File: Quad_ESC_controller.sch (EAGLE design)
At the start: 23 parts, among them Y1 ECS-80-S-4X

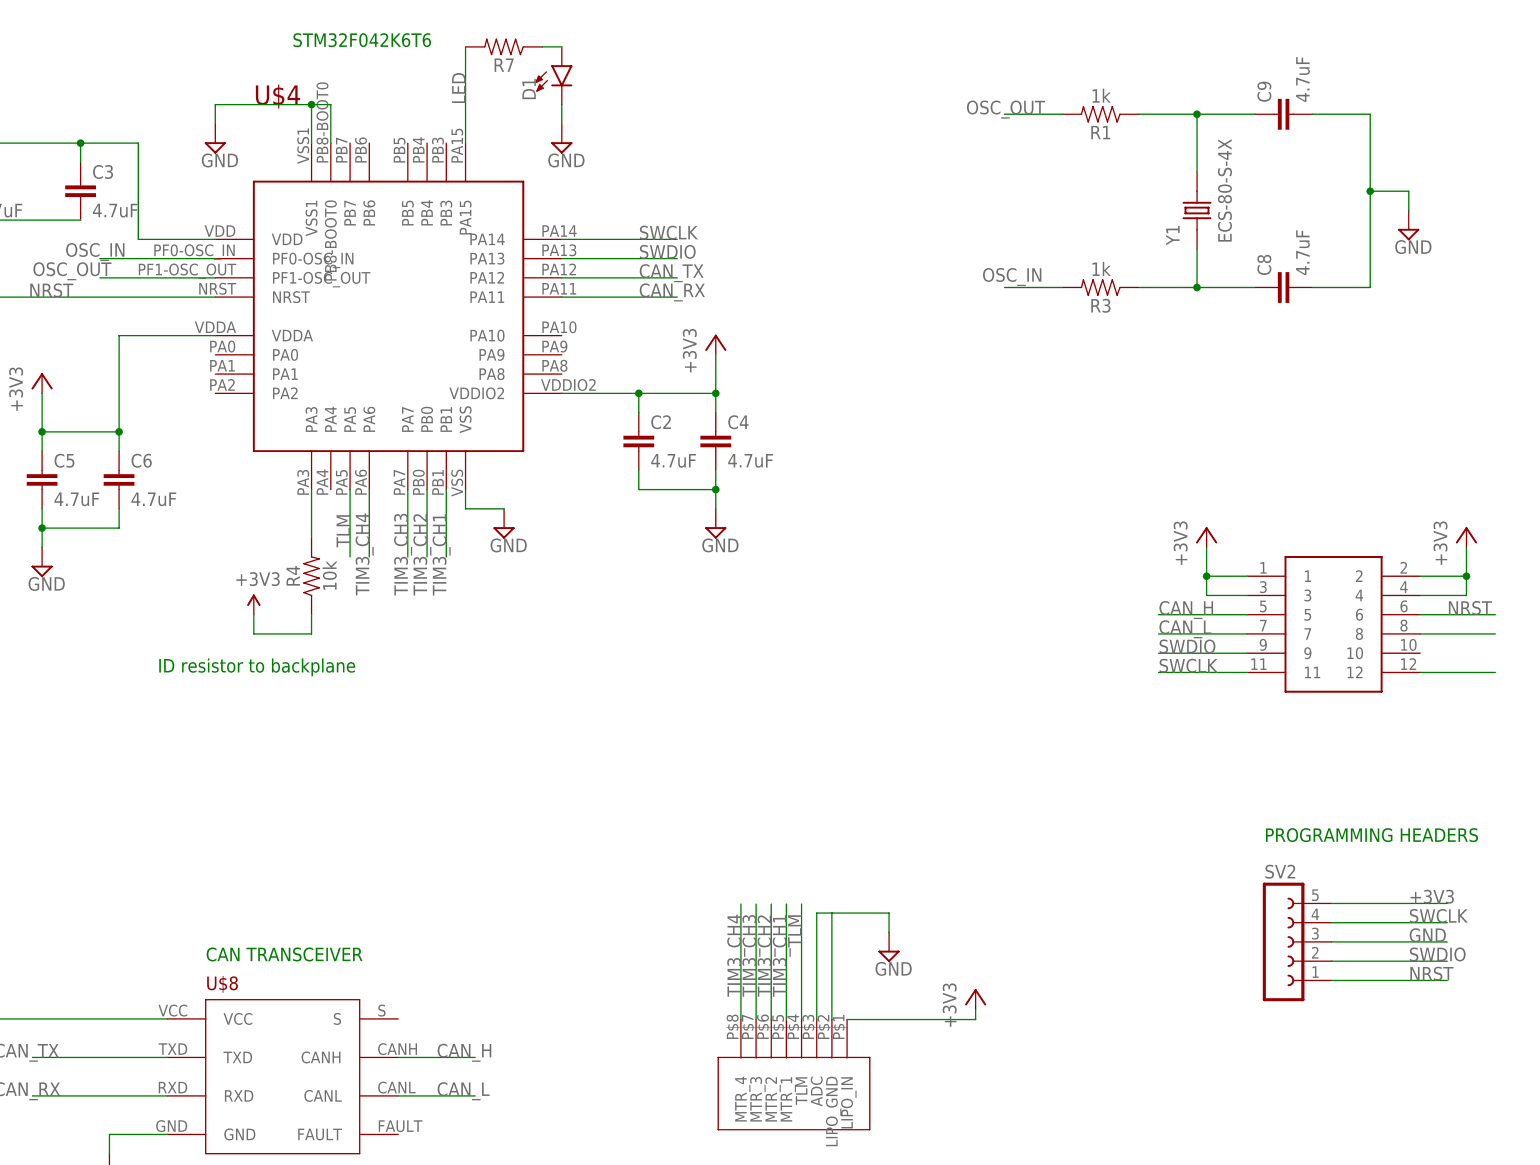
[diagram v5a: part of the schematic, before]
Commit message: Final Board Changes   ✽-(ˆ▿ˆ)/✽
thank god

(changes: vias con. to GND, esc id/tlm connections, design moved, connector footprint replaced, font sizes changed)
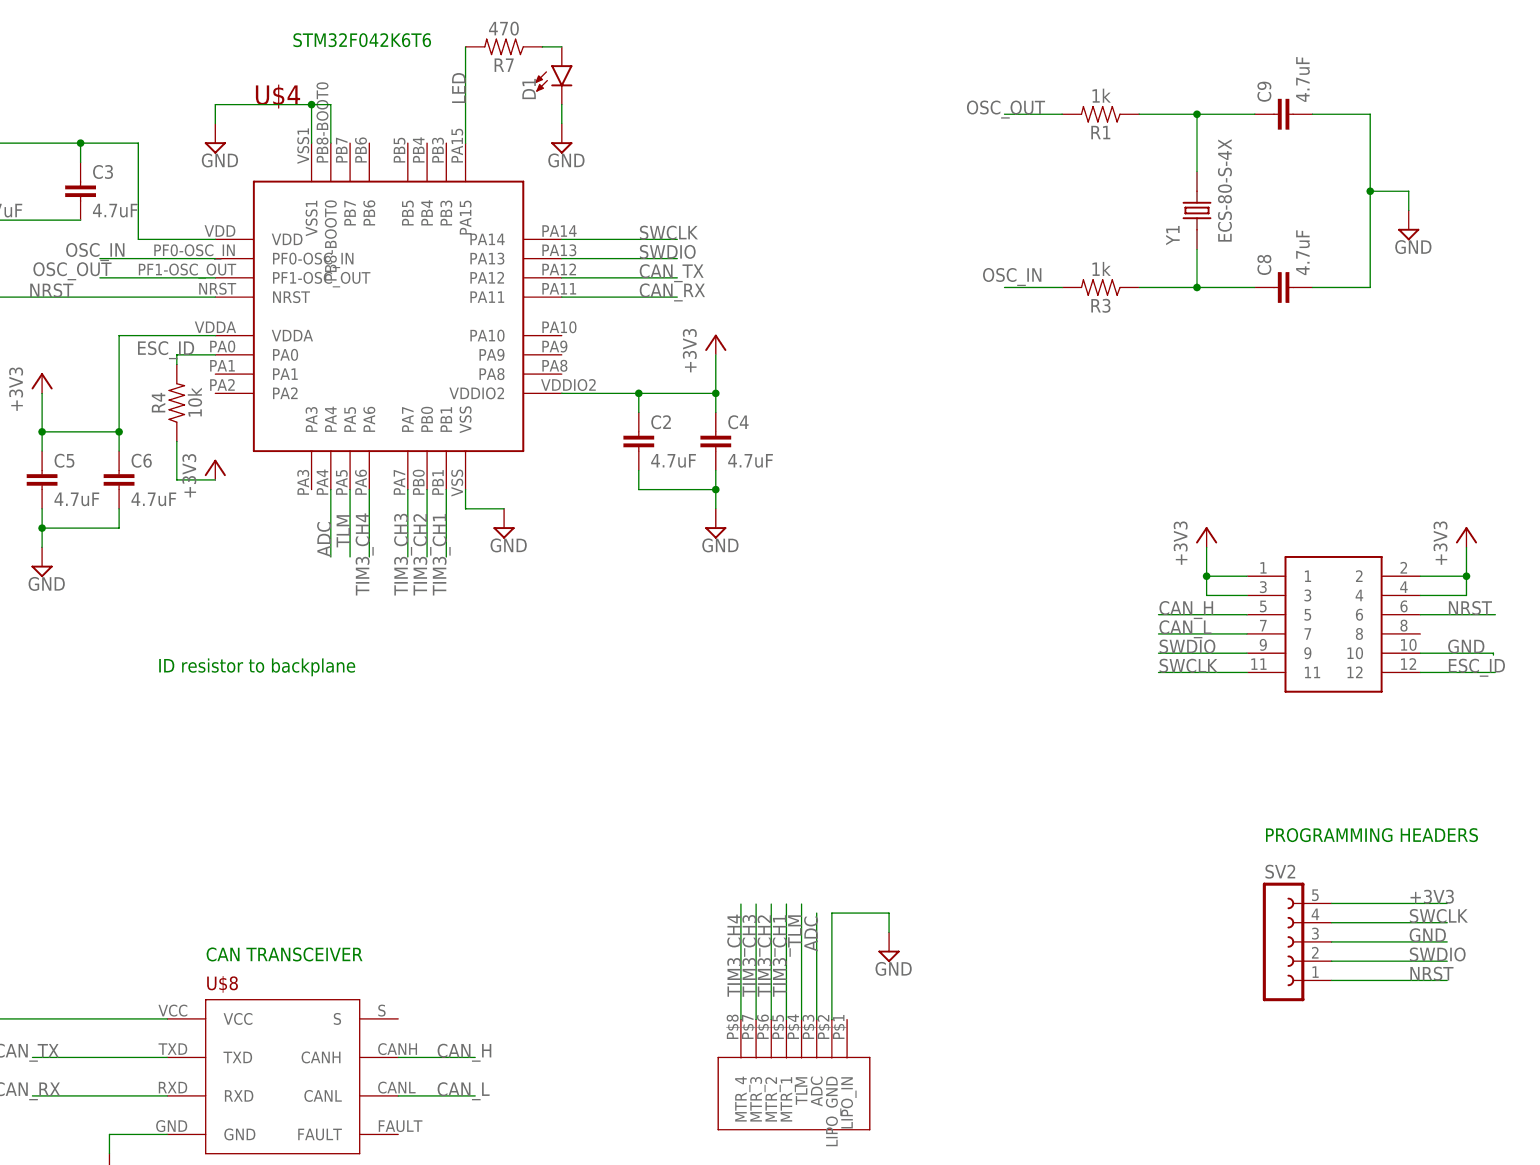
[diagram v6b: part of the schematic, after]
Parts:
- R7: value (none) -> 470
- RESET: value SWITCH -> DISCRETECOMPONENTS_SWITCH; device DiscreteComponents:SWITCH -> Push button - FSM2JMTR:DISCRETECOMPONENTS_SWITCH
- U$3: value BACKPLANE_CONNECTORSBKP -> BACKPLANE_CONNECTORSESC; device BLHeli_32 45A:BACKPLANE_CONNECTORSBKP -> BLHeli_32 45A:BACKPLANE_CONNECTORSESC
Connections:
- removed net N$3: R4.2, U$4.PA3
- removed net N$7: U$3.8
- removed net N$8: U$3.12
- new net ADC: U$2.ADC, U$4.PA4
- new net ESC_ID: R4.2, U$3.12, U$4.PA0
- net +3V3: no longer U$2.LIPO_IN
- net GND: now also U$3.10; no longer U$2.ADC
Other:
- moved on the sheet: R4

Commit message: JST part
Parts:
- C10: value 100nF -> 0.1uF
- C8, C9: value 4.7uF -> 20pF
- R1, R3: value 1k -> 0
- U$2: value 8PIN_CONNECTOR -> JST-8PIN; device BLHeli_32 45A:8PIN_CONNECTOR -> JST 8 pin:JST-8PIN
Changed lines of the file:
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@@
 <layers>
 <layer number="1" name="Top" color="4" fill="1" visible="no" active="no"/>
+<layer number="2" name="Route2" color="16" fill="1" visible="no" active="no"/>
+<layer number="3" name="Route3" color="17" fill="1" visible="no" active="no"/>
+<layer number="4" name="Route4" color="18" fill="1" visible="no" active="no"/>
+<layer number="5" name="Route5" color="19" fill="1" visible="no" active="no"/>
+<layer number="6" name="Route6" color="25" fill="1" visible="no" active="no"/>
+<layer number="7" name="Route7" color="26" fill="1" visible="no" active="no"/>
+<layer number="8" name="Route8" color="27" fill="1" visible="no" active="no"/>
+<layer number="9" name="Route9" color="28" fill="1" visible="no" active="no"/>
+<layer number="10" name="Route10" color="29" fill="1" visible="no" active="no"/>
+<layer number="11" name="Route11" color="30" fill="1" visible="no" active="no"/>
+<layer number="12" name="Route12" color="20" fill="1" visible="no" active="no"/>
+<layer number="13" name="Route13" color="21" fill="1" visible="no" active="no"/>
+<layer number="14" name="Route14" color="22" fill="1" visible="no" active="no"/>
+<layer number="15" name="Route15" color="23" fill="1" visible="no" active="no"/>
 <layer number="16" name="Bottom" color="1" fill="1" visible="no" active="no"/>
 <layer number="17" name="Pads" color="2" fill="1" visible="no" active="no"/>
@@
 <part name="SV2" library="con-lsta" library_urn="urn:adsk.eagle:library:161" deviceset="FE05-1" device="" package3d_urn="urn:adsk.eagle:package:8190/1"/>
 <part name="U$8" library="PI_Shield_Library" deviceset="TCAN337D" device=""/>
-<part name="C10" library="SparkFun-Capacitors" library_urn="urn:adsk.eagle:library:510" deviceset="4.7UF" device="0603" package3d_urn="urn:adsk.eagle:package:37414/1" value="100nF"/>
+<part name="C10" library="SparkFun-Capacitors" library_urn="urn:adsk.eagle:library:510" deviceset="4.7UF" device="0603" package3d_urn="urn:adsk.eagle:package:37414/1" value="0.1uF"/>
 <part name="+3V3" library="supply1" library_urn="urn:adsk.eagle:library:371" deviceset="+3V3" device=""/>
 <part name="GND9" library="supply2" library_urn="urn:adsk.eagle:library:372" deviceset="GND" device=""/>
 <part name="GND12" library="supply2" library_urn="urn:adsk.eagle:library:372" deviceset="GND" device=""/>
-<part name="C8" library="SparkFun-Capacitors" library_urn="urn:adsk.eagle:library:510" deviceset="4.7UF" device="0603" package3d_urn="urn:adsk.eagle:package:37414/1" value="4.7uF"/>
-<part name="C9" library="SparkFun-Capacitors" library_urn="urn:adsk.eagle:library:510" deviceset="4.7UF" device="0603" package3d_urn="urn:adsk.eagle:package:37414/1" value="4.7uF"/>
+<part name="C8" library="SparkFun-Capacitors" library_urn="urn:adsk.eagle:library:510" deviceset="4.7UF" device="0603" package3d_urn="urn:adsk.eagle:package:37414/1" value="20pF"/>
+<part name="C9" library="SparkFun-Capacitors" library_urn="urn:adsk.eagle:library:510" deviceset="4.7UF" device="0603" package3d_urn="urn:adsk.eagle:package:37414/1" value="20pF"/>
 <part name="Y1" library="ECS-80-S-4X" deviceset="ECS-80-S-4X" device=""/>
-<part name="R1" library="SparkFun-Resistors" library_urn="urn:adsk.eagle:library:532" deviceset="1KOHM" device="-0603-1/10W-1%" package3d_urn="urn:adsk.eagle:package:39650/1" value="1k"/>
-<part name="R3" library="SparkFun-Resistors" library_urn="urn:adsk.eagle:library:532" deviceset="1KOHM" device="-0603-1/10W-1%" package3d_urn="urn:adsk.eagle:package:39650/1" value="1k"/>
+<part name="R1" library="SparkFun-Resistors" library_urn="urn:adsk.eagle:library:532" deviceset="1KOHM" device="-0603-1/10W-1%" package3d_urn="urn:adsk.eagle:package:39650/1" value="0"/>
+<part name="R3" library="SparkFun-Resistors" library_urn="urn:adsk.eagle:library:532" deviceset="1KOHM" device="-0603-1/10W-1%" package3d_urn="urn:adsk.eagle:package:39650/1" value="0"/>
 <part name="GND15" library="supply2" library_urn="urn:adsk.eagle:library:372" deviceset="GND" device=""/>
 <part name="R4" library="SparkFun-Resistors" library_urn="urn:adsk.eagle:library:532" deviceset="10KOHM" device="-0603-1/10W-1%" package3d_urn="urn:adsk.eagle:package:39650/1" value="10k"/>
-<part name="U$2" library="BLHeli_32 45A" deviceset="8PIN_CONNECTOR" device=""/>
+<part name="U$2" library="JST 8 pin" deviceset="JST-8PIN" device="" package3d_urn="urn:adsk.eagle:package:25902943/3"/>
 <part name="U$3" library="BLHeli_32 45A" deviceset="BACKPLANE_CONNECTORS" device="ESC" value="BACKPLANE_CONNECTORSESC"/>
 <part name="+3V8" library="supply1" library_urn="urn:adsk.eagle:library:371" deviceset="+3V3" device=""/>
@@
 <attribute name="VALUE" x="59.944" y="124.46" size="1.778" layer="96" font="vector" rot="R90" align="top-center"/>
 </instance>
-<instance part="U$2" gate="G$1" x="149.86" y="38.1" smashed="yes" rot="R180"/>
+<instance part="U$2" gate="G$1" x="134.62" y="40.64" smashed="yes" rot="R180"/>
 <instance part="U$3" gate="G$1" x="210.82" y="95.25" smashed="yes"/>
 <instance part="+3V8" gate="G$1" x="194.31" y="107.95" smashed="yes">
@@
 <attribute name="VALUE" x="226.06" y="102.87" size="1.778" layer="96" rot="R90"/>
 </instance>
-<instance part="SUPPLY1" gate="GND" x="152.4" y="52.07" smashed="yes">
-<attribute name="VALUE" x="150.495" y="48.895" size="1.778" layer="96"/>
+<instance part="SUPPLY1" gate="GND" x="149.86" y="30.48" smashed="yes">
+<attribute name="VALUE" x="147.955" y="27.305" size="1.778" layer="96"/>
 </instance>
 <instance part="+3V6" gate="G$1" x="63.5" y="116.84" smashed="yes">
@@
 </segment>
 <segment>
-<wire x1="144.86" y1="57.15" x2="152.4" y2="57.15" width="0.1524" layer="91"/>
-<wire x1="152.4" y1="57.15" x2="152.4" y2="54.61" width="0.1524" layer="91"/>
+<wire x1="149.86" y1="43.18" x2="149.86" y2="33.02" width="0.1524" layer="91"/>
 <pinref part="U$2" gate="G$1" pin="LIPO_GND"/>
-<wire x1="144.86" y1="43.1" x2="144.86" y2="57.15" width="0.1524" layer="91"/>
+<wire x1="144.78" y1="43.18" x2="149.86" y2="43.18" width="0.1524" layer="91"/>
 <pinref part="SUPPLY1" gate="GND" pin="GND"/>
 </segment>
@@
 <segment>
 <pinref part="U$2" gate="G$1" pin="MTR_1"/>
-<wire x1="138.86" y1="43.1" x2="138.86" y2="58.34" width="0.1524" layer="91"/>
-<label x="138.86" y="57.07" size="1.778" layer="95" rot="R90" align="bottom-right"/>
+<wire x1="144.78" y1="50.8" x2="157.48" y2="50.8" width="0.1524" layer="91"/>
+<label x="157.48" y="50.8" size="1.778" layer="95" align="bottom-right"/>
 </segment>
 <segment>
@@
 <segment>
 <pinref part="U$2" gate="G$1" pin="MTR_2"/>
-<wire x1="136.86" y1="43.1" x2="136.86" y2="58.34" width="0.1524" layer="91"/>
-<label x="136.86" y="57.07" size="1.778" layer="95" rot="R90" align="bottom-right"/>
+<wire x1="144.78" y1="53.34" x2="157.48" y2="53.34" width="0.1524" layer="91"/>
+<label x="157.48" y="53.34" size="1.778" layer="95" align="bottom-right"/>
 </segment>
 <segment>
@@
 <segment>
 <pinref part="U$2" gate="G$1" pin="MTR_3"/>
-<wire x1="134.86" y1="43.1" x2="134.86" y2="58.34" width="0.1524" layer="91"/>
-<label x="134.86" y="57.07" size="1.778" layer="95" rot="R90" align="bottom-right"/>
+<wire x1="144.78" y1="55.88" x2="157.48" y2="55.88" width="0.1524" layer="91"/>
+<label x="157.48" y="55.88" size="1.778" layer="95" align="bottom-right"/>
 </segment>
 <segment>
@@
 <segment>
 <pinref part="U$2" gate="G$1" pin="MTR_4"/>
-<wire x1="132.86" y1="43.1" x2="132.86" y2="58.34" width="0.1524" layer="91"/>
-<label x="132.86" y="57.07" size="1.778" layer="95" rot="R90" align="bottom-right"/>
+<wire x1="144.78" y1="58.42" x2="157.48" y2="58.42" width="0.1524" layer="91"/>
+<label x="157.48" y="58.42" size="1.778" layer="95" align="bottom-right"/>
 </segment>
 <segment>
@@
 <segment>
 <pinref part="U$2" gate="G$1" pin="TLM"/>
-<wire x1="140.86" y1="43.1" x2="140.86" y2="58.34" width="0.1524" layer="91"/>
-<label x="140.86" y="57.07" size="1.778" layer="95" rot="R90" align="bottom-right"/>
+<wire x1="144.78" y1="48.26" x2="157.48" y2="48.26" width="0.1524" layer="91"/>
+<label x="157.48" y="48.26" size="1.778" layer="95" align="bottom-right"/>
 </segment>
 <segment>
@@
 <segment>
 <pinref part="U$2" gate="G$1" pin="ADC"/>
-<wire x1="142.86" y1="43.1" x2="142.86" y2="57.15" width="0.1524" layer="91"/>
-<label x="143.002" y="52.07" size="1.778" layer="95" rot="R90"/>
-</segment>
-</net>
+<wire x1="144.78" y1="45.72" x2="157.48" y2="45.72" width="0.1524" layer="91"/>
+<label x="152.4" y="45.72" size="1.778" layer="95"/>
+</segment>
+</net>

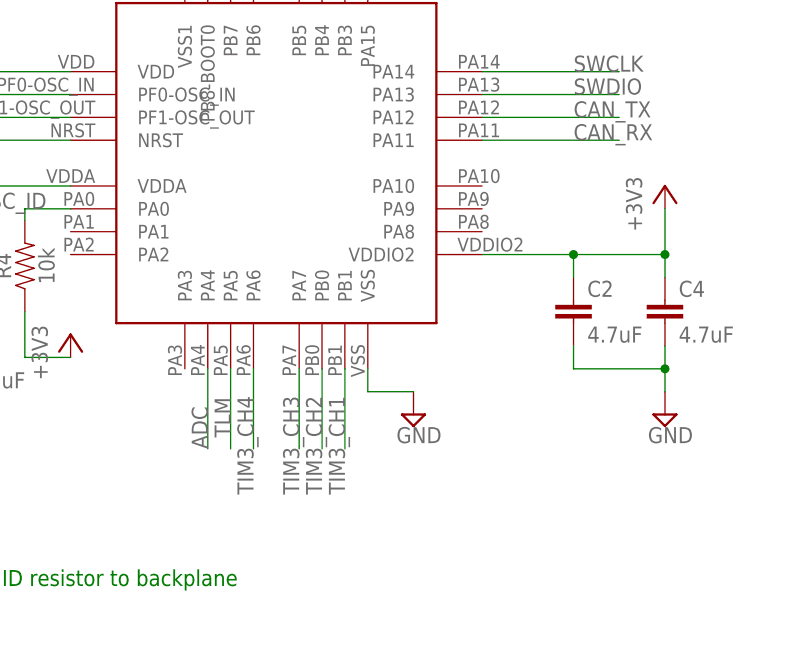
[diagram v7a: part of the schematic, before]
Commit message: Final Board Changes Pt. 2: Electric Boogaloo
Changes: [ bumped out board 100mil to the left, flipped esc signals on micro, moved TLM to analog pin 10 on micro, rotated connector, and rerouted board. ]
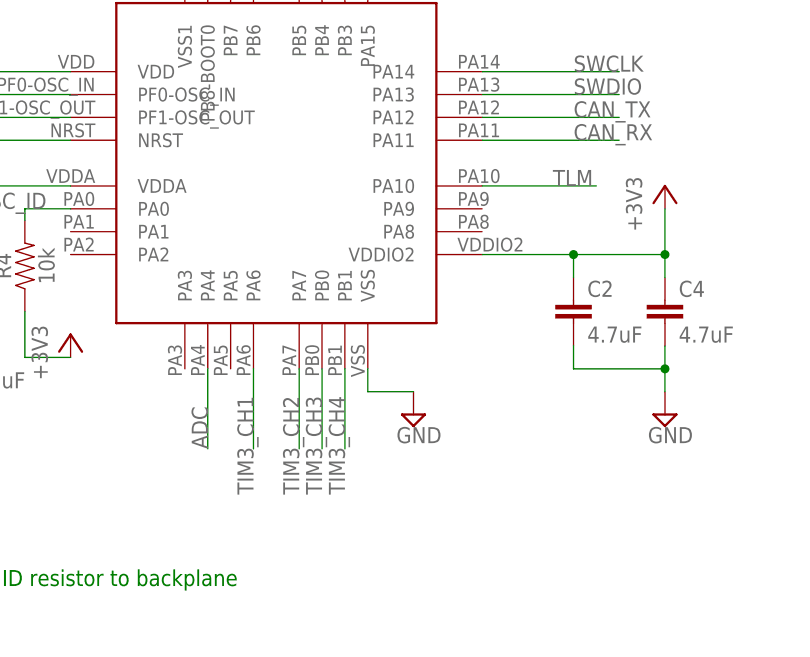
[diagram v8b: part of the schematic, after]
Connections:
- net TIM3_CH1: now also U$4.PA6; no longer U$4.PB1
- net TIM3_CH2: now also U$4.PA7; no longer U$4.PB0
- net TIM3_CH3: now also U$4.PB0; no longer U$4.PA7
- net TIM3_CH4: now also U$4.PB1; no longer U$4.PA6
- net TLM: now also U$4.PA10; no longer U$4.PA5
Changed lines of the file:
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@@
+</segment>
+<segment>
+<pinref part="U$4" gate="G$1" pin="PA6"/>
+<wire x1="83.82" y1="113.03" x2="83.82" y2="104.14" width="0.1524" layer="91"/>
+<label x="83.82" y="99.06" size="1.778" layer="95" rot="R90"/>
+</segment>
+</net>
+<net name="TIM3_CH2" class="0">
+<segment>
+<pinref part="U$2" gate="G$1" pin="MTR_2"/>
+<wire x1="144.78" y1="53.34" x2="157.48" y2="53.34" width="0.1524" layer="91"/>
+<label x="157.48" y="53.34" size="1.778" layer="95" align="bottom-right"/>
+</segment>
+<segment>
+<pinref part="U$4" gate="G$1" pin="PA7"/>
+<wire x1="88.9" y1="113.03" x2="88.9" y2="104.14" width="0.1524" layer="91"/>
+<label x="88.9" y="99.06" size="1.778" layer="95" rot="R90"/>
+</segment>
+</net>
+<net name="TIM3_CH3" class="0">
+<segment>
+<pinref part="U$2" gate="G$1" pin="MTR_3"/>
+<wire x1="144.78" y1="55.88" x2="157.48" y2="55.88" width="0.1524" layer="91"/>
+<label x="157.48" y="55.88" size="1.778" layer="95" align="bottom-right"/>
+</segment>
+<segment>
+<pinref part="U$4" gate="G$1" pin="PB0"/>
+<wire x1="91.44" y1="113.03" x2="91.44" y2="104.14" width="0.1524" layer="91"/>
+<label x="91.44" y="99.06" size="1.778" layer="95" rot="R90"/>
+</segment>
+</net>
+<net name="TIM3_CH4" class="0">
+<segment>
+<pinref part="U$2" gate="G$1" pin="MTR_4"/>
+<wire x1="144.78" y1="58.42" x2="157.48" y2="58.42" width="0.1524" layer="91"/>
+<label x="157.48" y="58.42" size="1.778" layer="95" align="bottom-right"/>
 </segment>
 <segment>
@@
 <wire x1="93.98" y1="113.03" x2="93.98" y2="104.14" width="0.1524" layer="91"/>
 <label x="93.98" y="99.06" size="1.778" layer="95" rot="R90"/>
-</segment>
-</net>
-<net name="TIM3_CH2" class="0">
-<segment>
-<pinref part="U$2" gate="G$1" pin="MTR_2"/>
-<wire x1="144.78" y1="53.34" x2="157.48" y2="53.34" width="0.1524" layer="91"/>
-<label x="157.48" y="53.34" size="1.778" layer="95" align="bottom-right"/>
-</segment>
-<segment>
-<pinref part="U$4" gate="G$1" pin="PB0"/>
-<wire x1="91.44" y1="113.03" x2="91.44" y2="104.14" width="0.1524" layer="91"/>
-<label x="91.44" y="99.06" size="1.778" layer="95" rot="R90"/>
-</segment>
-</net>
-<net name="TIM3_CH3" class="0">
-<segment>
-<pinref part="U$2" gate="G$1" pin="MTR_3"/>
-<wire x1="144.78" y1="55.88" x2="157.48" y2="55.88" width="0.1524" layer="91"/>
-<label x="157.48" y="55.88" size="1.778" layer="95" align="bottom-right"/>
-</segment>
-<segment>
-<pinref part="U$4" gate="G$1" pin="PA7"/>
-<wire x1="88.9" y1="113.03" x2="88.9" y2="104.14" width="0.1524" layer="91"/>
-<label x="88.9" y="99.06" size="1.778" layer="95" rot="R90"/>
-</segment>
-</net>
-<net name="TIM3_CH4" class="0">
-<segment>
-<pinref part="U$2" gate="G$1" pin="MTR_4"/>
-<wire x1="144.78" y1="58.42" x2="157.48" y2="58.42" width="0.1524" layer="91"/>
-<label x="157.48" y="58.42" size="1.778" layer="95" align="bottom-right"/>
-</segment>
-<segment>
-<pinref part="U$4" gate="G$1" pin="PA6"/>
-<wire x1="83.82" y1="113.03" x2="83.82" y2="104.14" width="0.1524" layer="91"/>
-<label x="83.82" y="99.06" size="1.778" layer="95" rot="R90"/>
 </segment>
 </net>
@@
 </segment>
 <segment>
-<pinref part="U$4" gate="G$1" pin="PA5"/>
-<wire x1="81.28" y1="113.03" x2="81.28" y2="104.14" width="0.1524" layer="91"/>
-<label x="81.28" y="105.41" size="1.778" layer="95" rot="R90"/>
-</segment>
-</net>
+<pinref part="U$4" gate="G$1" pin="PA10"/>
+<wire x1="109.22" y1="133.35" x2="121.92" y2="133.35" width="0.1524" layer="91"/>
+<label x="117.094" y="133.35" size="1.778" layer="95"/>
+</segment>
+</net>
